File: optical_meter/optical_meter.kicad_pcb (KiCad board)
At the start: 2 copper layers, 1 part, among them U1 Pico

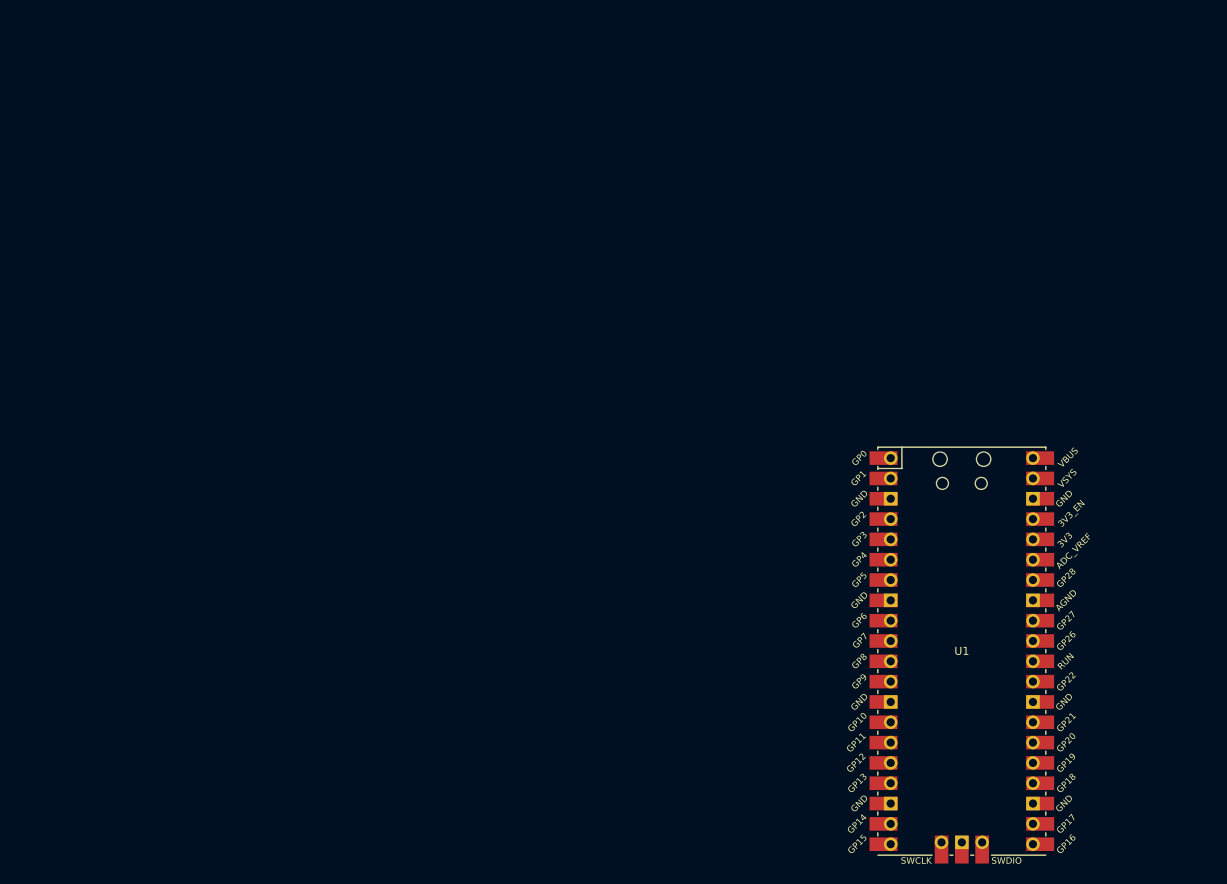
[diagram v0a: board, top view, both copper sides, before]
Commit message: Adding MH, Power OK diodes, new Goldping socket 3D model for RaspPi, SFP connectors with cage 3D model
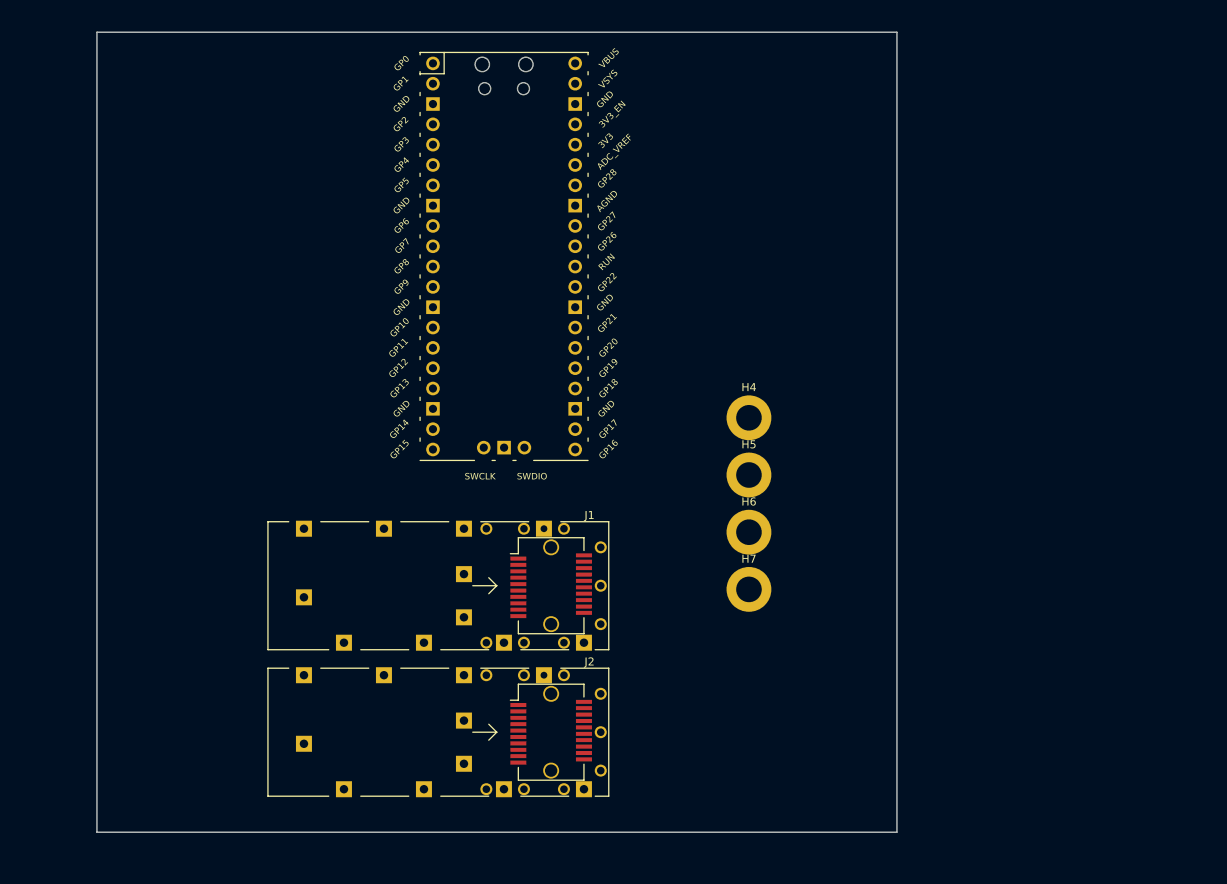
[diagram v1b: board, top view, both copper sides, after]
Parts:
- added H4: ~, MountingHole:MountingHole_3.2mm_M3_DIN965_Pad, F.Cu at (211.5, 68.2)
- added H5: ~, MountingHole:MountingHole_3.2mm_M3_DIN965_Pad, F.Cu at (211.5, 75.3)
- added H6: ~, MountingHole:MountingHole_3.2mm_M3_DIN965_Pad, F.Cu at (211.5, 82.5)
- added H7: ~, MountingHole:MountingHole_3.2mm_M3_DIN965_Pad, F.Cu at (211.5, 89.7)
- added J1: SFP+, SFP:Connector_SFP_and_Cage, F.Cu at (193.0, 89.2)
- added J2: SFP+, SFP:Connector_SFP_and_Cage, F.Cu at (193.0, 107.5)
- moved U1 75.6 mm to (180.9, 48.0)
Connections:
- U1 pad 13: unconnected-(U1-GND-Pad13) -> GND
- U1 pad 18: unconnected-(U1-GND-Pad18) -> GND
- U1 pad 23: unconnected-(U1-GND-Pad23) -> GND
- U1 pad 28: unconnected-(U1-GND-Pad28) -> GND
- U1 pad 3: unconnected-(U1-GND-Pad3) -> GND
- U1 pad 38: unconnected-(U1-GND-Pad38) -> GND
- U1 pad 40: unconnected-(U1-VBUS-Pad40) -> +5V
- U1 pad 42: unconnected-(U1-GND-Pad42) -> GND
- U1 pad 8: unconnected-(U1-GND-Pad8) -> GND
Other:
- board outline added: 100 x 100 mm

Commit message: Finished schematic (v1.0)
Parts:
- removed U1: Pico, MCU_RaspberryPi_and_Boards:RPi_Pico_SMD_TH
- added C1: 4u7, Capacitor_SMD:C_0603_1608Metric, F.Cu at (125.8, 75.6)
- added C10: 100n, Capacitor_SMD:C_0603_1608Metric, F.Cu at (129.8, 83.1)
- added C11: 100n, Capacitor_SMD:C_0603_1608Metric, F.Cu at (129.8, 85.6)
- added C12: 100n, Capacitor_SMD:C_0603_1608Metric, F.Cu at (129.8, 88.2)
- added C13: 100n, Capacitor_SMD:C_0603_1608Metric, F.Cu at (133.8, 75.6)
- added C14: 100n, Capacitor_SMD:C_0603_1608Metric, F.Cu at (133.8, 78.1)
- added C15: 100n, Capacitor_SMD:C_0603_1608Metric, F.Cu at (133.8, 80.6)
- added C16: 4u7, Capacitor_SMD:C_0603_1608Metric, F.Cu at (133.8, 83.1)
- added C17: 100n, Capacitor_SMD:C_0603_1608Metric, F.Cu at (212.4, 52.5)
- added C18: 4u7, Capacitor_SMD:C_0603_1608Metric, F.Cu at (212.4, 55.0)
- added C19: 4u7, Capacitor_SMD:C_0603_1608Metric, F.Cu at (212.4, 57.5)
- added C2: 100n, Capacitor_SMD:C_0603_1608Metric, F.Cu at (125.8, 78.1)
- added C3: 100n, Capacitor_SMD:C_0603_1608Metric, F.Cu at (125.8, 80.6)
- added C4: 100n, Capacitor_SMD:C_0603_1608Metric, F.Cu at (125.8, 83.1)
- added C5: 100n, Capacitor_SMD:C_0603_1608Metric, F.Cu at (125.8, 85.6)
- added C6: 100n, Capacitor_SMD:C_0603_1608Metric, F.Cu at (125.8, 88.2)
- added C7: 4u7, Capacitor_SMD:C_0603_1608Metric, F.Cu at (129.8, 75.6)
- added C8: 100n, Capacitor_SMD:C_0603_1608Metric, F.Cu at (129.8, 78.1)
- added C9: 100n, Capacitor_SMD:C_0603_1608Metric, F.Cu at (129.8, 80.6)
- added D1: LED, Diode_SMD:D_0603_1608Metric, F.Cu at (137.9, 94.6)
- added D2: LED, Diode_SMD:D_0603_1608Metric, F.Cu at (137.9, 97.2)
- added J3: Conn_01x02_Pin, Connector_PinHeader_2.54mm:PinHeader_1x02_P2.54mm_Vertical, F.Cu at (138.2, 88.5)
- added J4: Conn_02x03, Connector_PinHeader_2.54mm:PinHeader_2x03_P2.54mm_Vertical, F.Cu at (205.6, 53.6)
- added L1: 1u, Inductor_SMD:L_0805_2012Metric_Pad1.15x1.40mm_HandSolder, F.Cu at (138.2, 75.8)
- added L2: 1u, Inductor_SMD:L_0805_2012Metric_Pad1.15x1.40mm_HandSolder, F.Cu at (138.2, 78.8)
- added L3: 1u, Inductor_SMD:L_0805_2012Metric_Pad1.15x1.40mm_HandSolder, F.Cu at (138.2, 81.7)
- added L4: 1u, Inductor_SMD:L_0805_2012Metric_Pad1.15x1.40mm_HandSolder, F.Cu at (138.2, 84.7)
- added R1: 1k, Resistor_SMD:R_0603_1608Metric_Pad0.98x0.95mm_HandSolder, F.Cu at (121.6, 75.6)
- added R10: 100, Resistor_SMD:R_0603_1608Metric_Pad0.98x0.95mm_HandSolder, F.Cu at (121.6, 95.7)
- added R11: 4k7, Resistor_SMD:R_0603_1608Metric_Pad0.98x0.95mm_HandSolder, F.Cu at (121.6, 98.2)
- added R2: 1k, Resistor_SMD:R_0603_1608Metric_Pad0.98x0.95mm_HandSolder, F.Cu at (121.6, 78.1)
- added R3: 4k7, Resistor_SMD:R_0603_1608Metric_Pad0.98x0.95mm_HandSolder, F.Cu at (121.6, 80.6)
- added R4: 4k7, Resistor_SMD:R_0603_1608Metric_Pad0.98x0.95mm_HandSolder, F.Cu at (121.6, 83.1)
- added R5: 4k7, Resistor_SMD:R_0603_1608Metric_Pad0.98x0.95mm_HandSolder, F.Cu at (216.6, 52.5)
- added R6: 4k7, Resistor_SMD:R_0603_1608Metric_Pad0.98x0.95mm_HandSolder, F.Cu at (121.6, 85.6)
- added R7: 4k7, Resistor_SMD:R_0603_1608Metric_Pad0.98x0.95mm_HandSolder, F.Cu at (121.6, 88.2)
- added R8: 4k7, Resistor_SMD:R_0603_1608Metric_Pad0.98x0.95mm_HandSolder, F.Cu at (121.6, 90.7)
- added R9: 100, Resistor_SMD:R_0603_1608Metric_Pad0.98x0.95mm_HandSolder, F.Cu at (121.6, 93.2)
- added S1: SW Push, SW_Push:434123025816, F.Cu at (215.2, 71.5)
- added U2: FIN1002M5X, LVDS_RX_lib:SOT95P280X140-5N, F.Cu at (213.4, 78.3)
- added U3: FIN1001M5X, LVDS_RX_lib:SOT95P280X140-5N, F.Cu at (213.4, 82.5)
- added U4: Pico, MCU_RaspberryPi_and_Boards:RPi_Pico_SMD_TH, F.Cu at (191.7, 64.3)
- moved J2 48.5 mm to (169.2, 65.2)
- moved J1 48.5 mm to (169.2, 46.9)
- moved H4 45.7 mm to (174.5, 41.3)
- moved H5 45.7 mm to (174.5, 48.5)
- moved H6 45.7 mm to (174.5, 55.6)
- moved H7 45.7 mm to (174.5, 62.8)
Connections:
- J1 pad 1: Net-(J1-VeeT-Pad1) -> GND
- J1 pad 10: Net-(J1-VeeR-Pad10) -> GND
- J1 pad 11: Net-(J1-VeeR-Pad10) -> GND
- J1 pad 14: Net-(J1-VeeR-Pad10) -> GND
- J1 pad 15: unconnected-(J1-VccR-Pad15) -> Net-(J1-VccR)
- J1 pad 16: unconnected-(J1-VccT-Pad16) -> Net-(J1-VccT)
- J1 pad 17: Net-(J1-VeeT-Pad1) -> GND
- J1 pad 18: unconnected-(J1-TD+-Pad18) -> /TD0+
- J1 pad 19: unconnected-(J1-TD--Pad19) -> /TD0-
- J1 pad 2: unconnected-(J1-TX_FAULT-Pad2) -> Net-(J1-TX_FAULT)
- J1 pad 20: Net-(J1-VeeT-Pad1) -> GND
- J1 pad 3: unconnected-(J1-TX_DISABLE-Pad3) -> /TX_DISABLE0
- J1 pad 4: unconnected-(J1-SDA-Pad4) -> /SDA0
- J1 pad 5: unconnected-(J1-SCL-Pad5) -> /SCL0
- J1 pad 6: unconnected-(J1-MOD_ABS-Pad6) -> GND
- J1 pad 7: unconnected-(J1-RS0-Pad7) -> /RS00
- J1 pad 8: unconnected-(J1-RX_LOS-Pad8) -> Net-(J1-RX_LOS)
- J1 pad 9: unconnected-(J1-RS1-Pad9) -> /RS10
- J1 pad CAGE: unconnected-(J1-PadCAGE) -> GND
- J2 pad 1: Net-(J2-VeeT-Pad1) -> GND
- J2 pad 10: Net-(J2-VeeR-Pad10) -> GND
- J2 pad 11: Net-(J2-VeeR-Pad10) -> GND
- J2 pad 12: unconnected-(J2-RD--Pad12) -> /RD1-
- J2 pad 13: unconnected-(J2-RD+-Pad13) -> /RD1+
- J2 pad 14: Net-(J2-VeeR-Pad10) -> GND
- J2 pad 15: unconnected-(J2-VccR-Pad15) -> Net-(J2-VccR)
- J2 pad 16: unconnected-(J2-VccT-Pad16) -> Net-(J2-VccT)
- J2 pad 17: Net-(J2-VeeT-Pad1) -> GND
- J2 pad 2: unconnected-(J2-TX_FAULT-Pad2) -> Net-(J2-TX_FAULT)
- J2 pad 20: Net-(J2-VeeT-Pad1) -> GND
- J2 pad 3: unconnected-(J2-TX_DISABLE-Pad3) -> /TX_DISABLE1
- J2 pad 4: unconnected-(J2-SDA-Pad4) -> /SDA1
- J2 pad 5: unconnected-(J2-SCL-Pad5) -> /SCL1
- J2 pad 6: unconnected-(J2-MOD_ABS-Pad6) -> GND
- J2 pad 7: unconnected-(J2-RS0-Pad7) -> /RS01
- J2 pad 8: unconnected-(J2-RX_LOS-Pad8) -> Net-(J2-RX_LOS)
- J2 pad 9: unconnected-(J2-RS1-Pad9) -> /RS11
- J2 pad CAGE: unconnected-(J2-PadCAGE) -> GND
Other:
- board outline removed

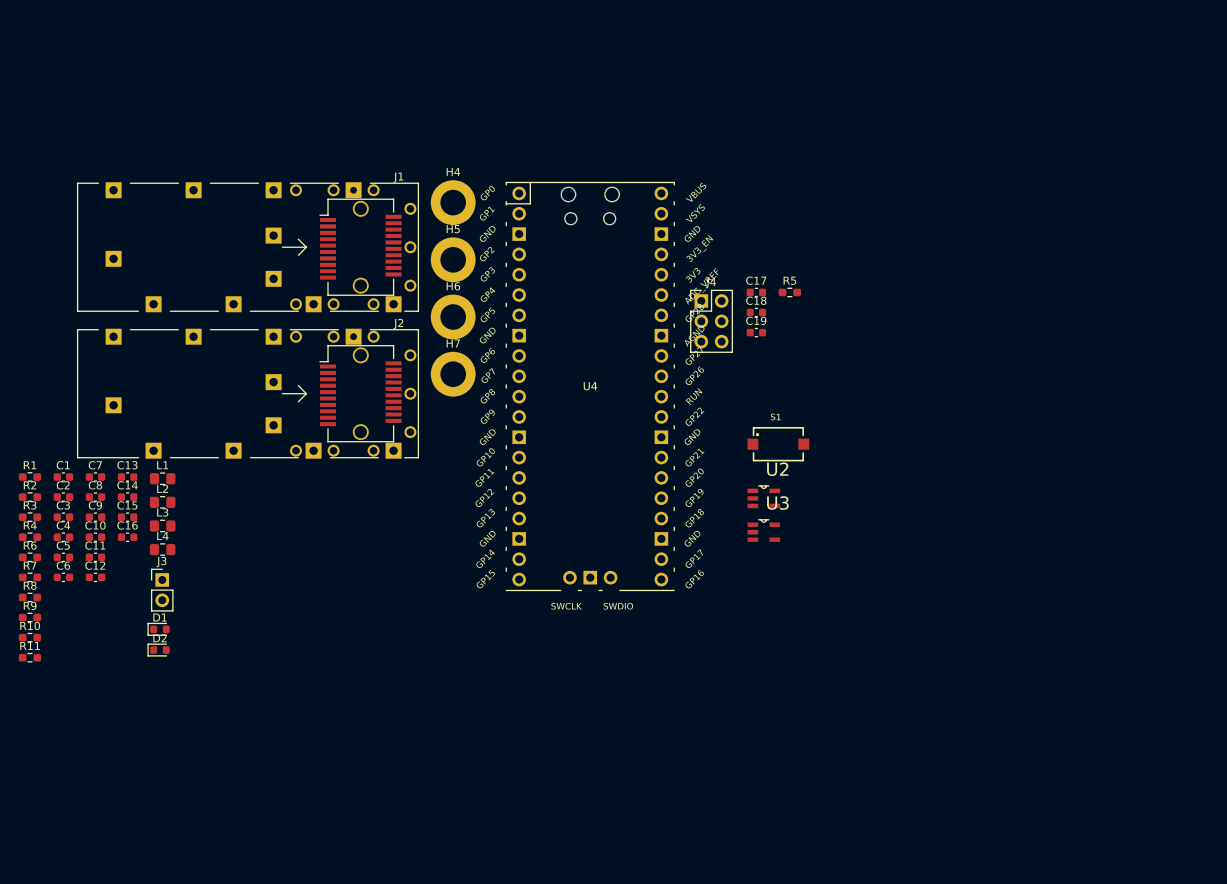
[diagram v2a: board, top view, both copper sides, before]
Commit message: Adding components to PCB
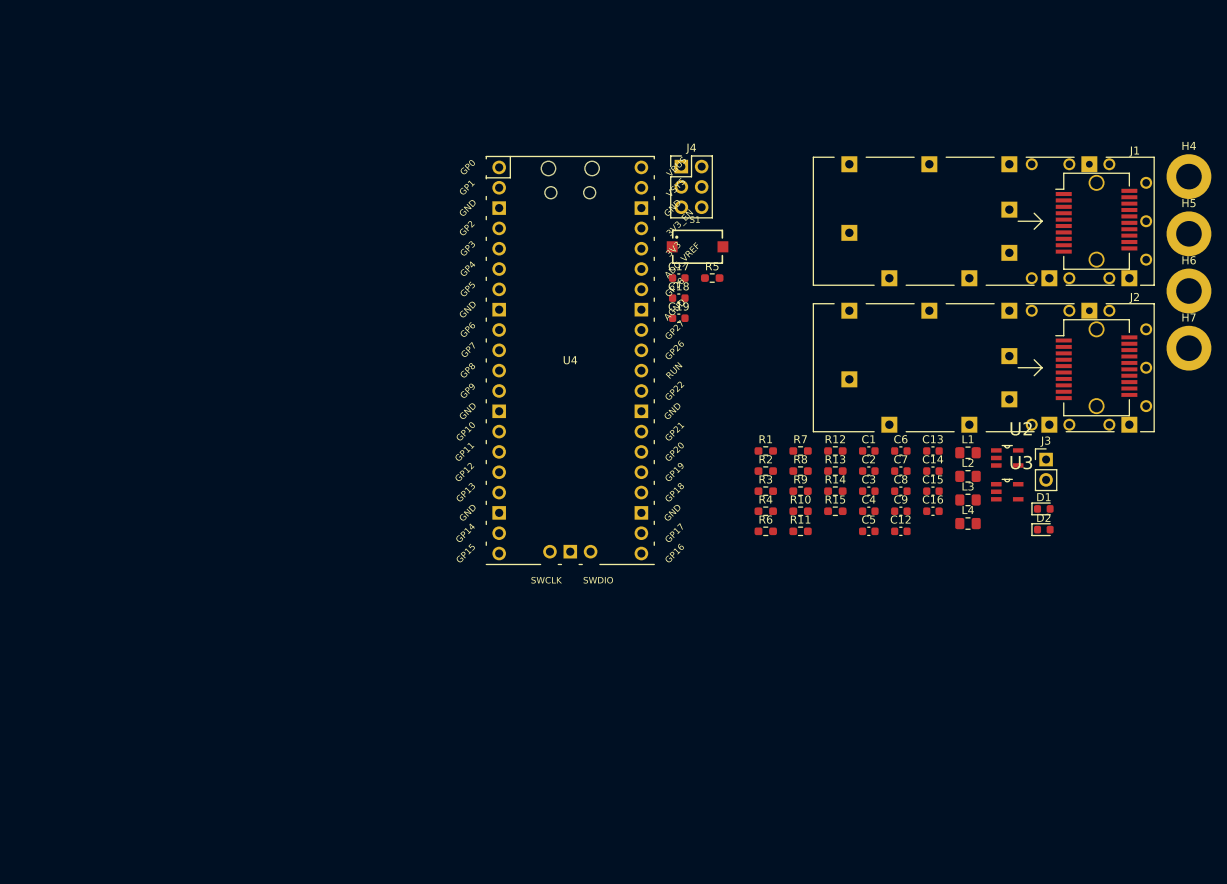
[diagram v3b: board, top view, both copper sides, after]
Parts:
- removed C10, C11: 100n, Capacitor_SMD:C_0603_1608Metric
- added R12: 137R, Resistor_SMD:R_0603_1608Metric_Pad0.98x0.95mm_HandSolder, F.Cu at (222.3, 72.3)
- added R13: 78R, Resistor_SMD:R_0603_1608Metric_Pad0.98x0.95mm_HandSolder, F.Cu at (222.3, 74.9)
- added R14: 137R, Resistor_SMD:R_0603_1608Metric_Pad0.98x0.95mm_HandSolder, F.Cu at (222.3, 77.4)
- added R15: 78R, Resistor_SMD:R_0603_1608Metric_Pad0.98x0.95mm_HandSolder, F.Cu at (222.3, 79.9)
- moved D1 111.5 mm to (248.4, 79.6)
- moved D2 111.5 mm to (248.4, 82.2)
- moved J3 111.5 mm to (248.6, 73.4)
- moved C6 105.9 mm to (230.5, 72.3)
- moved C12 100.8 mm to (230.5, 82.4)
- moved C1 100.7 mm to (226.5, 72.3)
- moved C13 100.7 mm to (234.5, 72.3)
- moved C14 100.7 mm to (234.5, 74.9)
- moved C15 100.7 mm to (234.5, 77.4)
- moved C16 100.7 mm to (234.5, 79.9)
- moved C2 100.7 mm to (226.5, 74.9)
- moved C3 100.7 mm to (226.5, 77.4)
- moved C4 100.7 mm to (226.5, 79.9)
- moved C5 100.7 mm to (226.5, 82.4)
- moved L1 100.7 mm to (238.9, 72.6)
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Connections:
- C12 pad 1: Net-(U2-RIN-) -> /RD1+
- C12 pad 2: /RD1- -> Net-(U2-RIN+)
- C13 pad 1: Net-(U2-RIN+) -> /RD1-
- C13 pad 2: /RD1+ -> Net-(U2-RIN-)
- J1 pad 2: Net-(J1-TX_FAULT) -> /TX_FAULT0
- J1 pad 8: Net-(J1-RX_LOS) -> /RX_LOS0
- J2 pad 2: Net-(J2-TX_FAULT) -> /TX_FAULT1
- J2 pad 8: Net-(J2-RX_LOS) -> /RX_LOS1
- J4 pad 2: +3V3 -> +5V
- R3 pad 2: Net-(J1-TX_FAULT) -> /TX_FAULT0
- R4 pad 1: Net-(J1-RX_LOS) -> /RX_LOS0
- R7 pad 1: Net-(J2-RX_LOS) -> /RX_LOS1
- R8 pad 1: +3V3 -> unconnected-(R8-Pad1)
- R8 pad 2: Net-(J2-TX_FAULT) -> /TX_FAULT1
- R9 pad 1: Net-(U3-DOUT+) -> /TD0+
- R9 pad 2: Net-(U3-DOUT-) -> /TD0-
- U3 pad 3: Net-(U3-DOUT-) -> /TD0-
- U3 pad 4: Net-(U3-DOUT+) -> /TD0+
- U4 pad 12: +3V3 -> /TX_FAULT1
- U4 pad 16: +3V3 -> /RX_LOS0
- U4 pad 20: +3V3 -> /TX_FAULT0
- U4 pad 9: +3V3 -> /RX_LOS1
